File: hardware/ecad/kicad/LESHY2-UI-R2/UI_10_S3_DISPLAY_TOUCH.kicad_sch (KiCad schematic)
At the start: 35 parts, among them J1 Hirose FH34SRJ-50S-0.5SH(50), J2 Samtec FTSH-105-01-L-DV-K-P-TR, J3 GCT RFPC-SMA32-FN-175-A, J4 Hirose U.FL-R-SMT-1(80), SW1 Alps Alpine SKRTLAE010, SW2 Alps Alpine SKRTLAE010, U1 ESP32-S3-WROOM-1U-N16R8, U2 Texas Instruments TPD4E05U06D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, U3 KYOCERA AVX CP0603Q5425ENTR

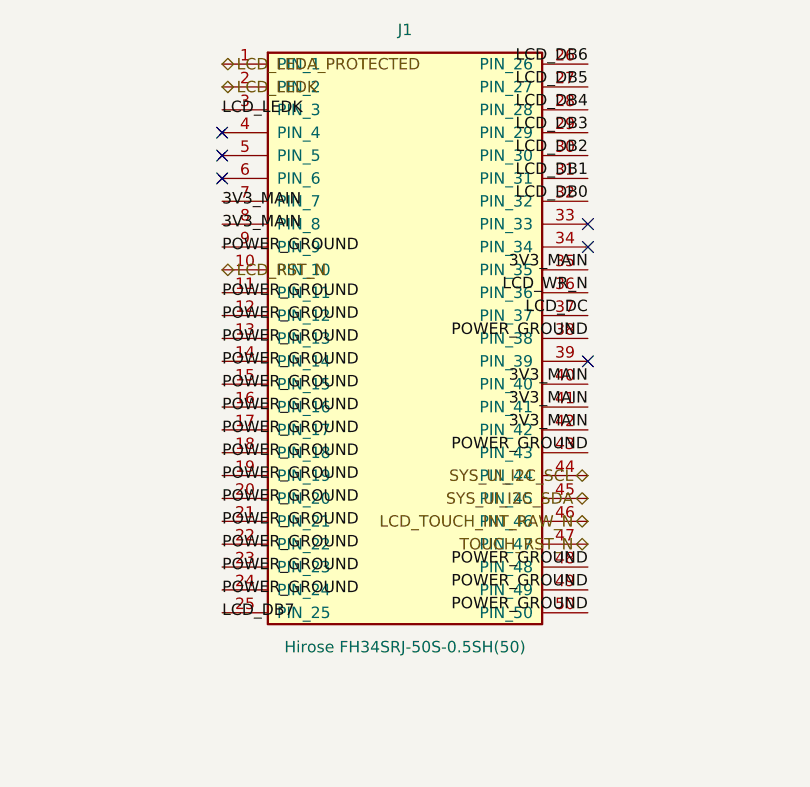
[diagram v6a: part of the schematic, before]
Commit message: Correct exact connector and protection geometry; expand electrical review
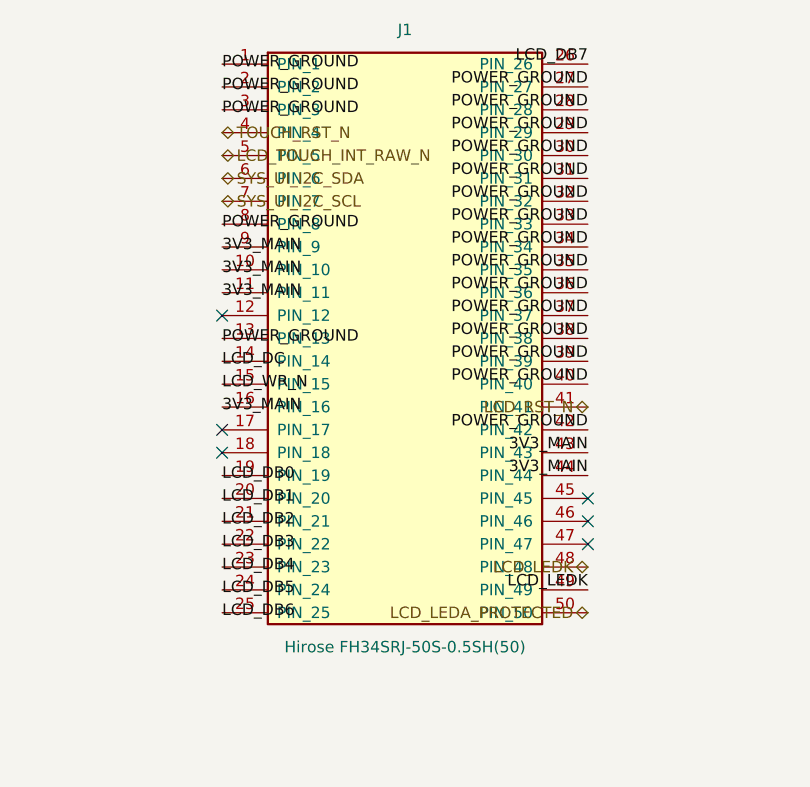
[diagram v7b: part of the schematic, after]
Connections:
- net 3V3_MAIN: now also J1.10 (PIN_10), J1.11 (PIN_11), J1.16 (PIN_16), J1.43 (PIN_43), J1.44 (PIN_44), J1.9 (PIN_9); no longer J1.35 (PIN_35), J1.40 (PIN_40), J1.41 (PIN_41), J1.42 (PIN_42), J1.7 (PIN_7), J1.8 (PIN_8)
- net LCD_DB0: now also J1.19 (PIN_19); no longer J1.32 (PIN_32)
- net LCD_DB1: now also J1.20 (PIN_20); no longer J1.31 (PIN_31)
- net LCD_DB2: now also J1.21 (PIN_21); no longer J1.30 (PIN_30)
- net LCD_DB3: now also J1.22 (PIN_22); no longer J1.29 (PIN_29)
- net LCD_DB4: now also J1.23 (PIN_23); no longer J1.28 (PIN_28)
- net LCD_DB5: now also J1.24 (PIN_24); no longer J1.27 (PIN_27)
- net LCD_DB6: now also J1.25 (PIN_25); no longer J1.26 (PIN_26)
- net LCD_DB7: now also J1.26 (PIN_26); no longer J1.25 (PIN_25)
- net LCD_DC: now also J1.14 (PIN_14); no longer J1.37 (PIN_37)
- net LCD_LEDA_PROTECTED: now also J1.50 (PIN_50); no longer J1.1 (PIN_1)
- net LCD_LEDK: now also J1.48 (PIN_48), J1.49 (PIN_49); no longer J1.2 (PIN_2), J1.3 (PIN_3)
- net LCD_RST_N: now also J1.41 (PIN_41); no longer J1.10 (PIN_10)
- net LCD_TOUCH_INT_RAW_N: now also J1.5 (PIN_5); no longer J1.46 (PIN_46)
- net LCD_WR_N: now also J1.15 (PIN_15); no longer J1.36 (PIN_36)
- net POWER_GROUND: now also J1.1 (PIN_1), J1.2 (PIN_2), J1.27 (PIN_27), J1.28 (PIN_28), J1.29 (PIN_29), J1.3 (PIN_3), J1.30 (PIN_30), J1.31 (PIN_31), J1.32 (PIN_32), J1.33 (PIN_33), J1.34 (PIN_34), J1.35 (PIN_35), J1.36 (PIN_36), J1.37 (PIN_37), J1.39 (PIN_39), J1.40 (PIN_40), J1.42 (PIN_42), J1.8 (PIN_8); no longer J1.11 (PIN_11), J1.12 (PIN_12), J1.14 (PIN_14), J1.15 (PIN_15), J1.16 (PIN_16), J1.17 (PIN_17), J1.18 (PIN_18), J1.19 (PIN_19), J1.20 (PIN_20), J1.21 (PIN_21), J1.22 (PIN_22), J1.23 (PIN_23), J1.24 (PIN_24), J1.43 (PIN_43), J1.48 (PIN_48), J1.49 (PIN_49), J1.50 (PIN_50), J1.9 (PIN_9)
- net SYS_UI_I2C_SCL: now also J1.7 (PIN_7); no longer J1.44 (PIN_44)
- net SYS_UI_I2C_SDA: now also J1.6 (PIN_6); no longer J1.45 (PIN_45)
- net TOUCH_RST_N: now also J1.4 (PIN_4); no longer J1.47 (PIN_47)
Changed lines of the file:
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@@
 		)
 	)
-	(hierarchical_label "LCD_LEDA_PROTECTED"
-		(shape bidirectional)
+	(label "POWER_GROUND"
 		(at 584.20 48.26 0)
 		(effects (font (size 1.27 1.27)))
 	)
-	(hierarchical_label "LCD_LEDK"
-		(shape bidirectional)
+	(label "POWER_GROUND"
 		(at 584.20 50.80 0)
 		(effects (font (size 1.27 1.27)))
 	)
-	(label "LCD_LEDK"
+	(label "POWER_GROUND"
 		(at 584.20 53.34 0)
 		(effects (font (size 1.27 1.27)))
 	)
-	(no_connect (at 584.20 55.88)
+	(hierarchical_label "TOUCH_RST_N"
+		(shape bidirectional)
+		(at 584.20 55.88 0)
+		(effects (font (size 1.27 1.27)))
 	)
-	(no_connect (at 584.20 58.42)
+	(hierarchical_label "LCD_TOUCH_INT_RAW_N"
+		(shape bidirectional)
+		(at 584.20 58.42 0)
+		(effects (font (size 1.27 1.27)))
 	)
-	(no_connect (at 584.20 60.96)
+	(hierarchical_label "SYS_UI_I2C_SDA"
+		(shape bidirectional)
+		(at 584.20 60.96 0)
+		(effects (font (size 1.27 1.27)))
 	)
-	(label "3V3_MAIN"
+	(hierarchical_label "SYS_UI_I2C_SCL"
+		(shape bidirectional)
 		(at 584.20 63.50 0)
 		(effects (font (size 1.27 1.27)))
 	)
-	(label "3V3_MAIN"
+	(label "POWER_GROUND"
 		(at 584.20 66.04 0)
 		(effects (font (size 1.27 1.27)))
 	)
-	(label "POWER_GROUND"
+	(label "3V3_MAIN"
 		(at 584.20 68.58 0)
 		(effects (font (size 1.27 1.27)))
 	)
-	(hierarchical_label "LCD_RST_N"
-		(shape bidirectional)
+	(label "3V3_MAIN"
 		(at 584.20 71.12 0)
 		(effects (font (size 1.27 1.27)))
 	)
-	(label "POWER_GROUND"
+	(label "3V3_MAIN"
 		(at 584.20 73.66 0)
 		(effects (font (size 1.27 1.27)))
 	)
-	(label "POWER_GROUND"
-		(at 584.20 76.20 0)
-		(effects (font (size 1.27 1.27)))
+	(no_connect (at 584.20 76.20)
 	)
 	(label "POWER_GROUND"
@@
 		(effects (font (size 1.27 1.27)))
 	)
-	(label "POWER_GROUND"
+	(label "LCD_DC"
 		(at 584.20 81.28 0)
 		(effects (font (size 1.27 1.27)))
 	)
-	(label "POWER_GROUND"
+	(label "LCD_WR_N"
 		(at 584.20 83.82 0)
 		(effects (font (size 1.27 1.27)))
 	)
-	(label "POWER_GROUND"
+	(label "3V3_MAIN"
 		(at 584.20 86.36 0)
 		(effects (font (size 1.27 1.27)))
 	)
-	(label "POWER_GROUND"
-		(at 584.20 88.90 0)
-		(effects (font (size 1.27 1.27)))
+	(no_connect (at 584.20 88.90)
 	)
-	(label "POWER_GROUND"
-		(at 584.20 91.44 0)
-		(effects (font (size 1.27 1.27)))
+	(no_connect (at 584.20 91.44)
 	)
-	(label "POWER_GROUND"
+	(label "LCD_DB0"
 		(at 584.20 93.98 0)
 		(effects (font (size 1.27 1.27)))
 	)
-	(label "POWER_GROUND"
+	(label "LCD_DB1"
 		(at 584.20 96.52 0)
 		(effects (font (size 1.27 1.27)))
 	)
-	(label "POWER_GROUND"
+	(label "LCD_DB2"
 		(at 584.20 99.06 0)
 		(effects (font (size 1.27 1.27)))
 	)
-	(label "POWER_GROUND"
+	(label "LCD_DB3"
 		(at 584.20 101.60 0)
 		(effects (font (size 1.27 1.27)))
 	)
-	(label "POWER_GROUND"
+	(label "LCD_DB4"
 		(at 584.20 104.14 0)
 		(effects (font (size 1.27 1.27)))
 	)
-	(label "POWER_GROUND"
+	(label "LCD_DB5"
 		(at 584.20 106.68 0)
 		(effects (font (size 1.27 1.27)))
 	)
-	(label "LCD_DB7"
+	(label "LCD_DB6"
 		(at 584.20 109.22 0)
 		(effects (font (size 1.27 1.27)))
 	)
-	(label "LCD_DB6"
+	(label "LCD_DB7"
 		(at 624.84 48.26 180)
 		(effects (font (size 1.27 1.27)) (justify right bottom))
 	)
-	(label "LCD_DB5"
+	(label "POWER_GROUND"
 		(at 624.84 50.80 180)
 		(effects (font (size 1.27 1.27)) (justify right bottom))
 	)
-	(label "LCD_DB4"
+	(label "POWER_GROUND"
 		(at 624.84 53.34 180)
 		(effects (font (size 1.27 1.27)) (justify right bottom))
 	)
-	(label "LCD_DB3"
+	(label "POWER_GROUND"
 		(at 624.84 55.88 180)
 		(effects (font (size 1.27 1.27)) (justify right bottom))
 	)
-	(label "LCD_DB2"
+	(label "POWER_GROUND"
 		(at 624.84 58.42 180)
 		(effects (font (size 1.27 1.27)) (justify right bottom))
 	)
-	(label "LCD_DB1"
+	(label "POWER_GROUND"
 		(at 624.84 60.96 180)
 		(effects (font (size 1.27 1.27)) (justify right bottom))
 	)
-	(label "LCD_DB0"
+	(label "POWER_GROUND"
 		(at 624.84 63.50 180)
 		(effects (font (size 1.27 1.27)) (justify right bottom))
 	)
-	(no_connect (at 624.84 66.04)
+	(label "POWER_GROUND"
+		(at 624.84 66.04 180)
+		(effects (font (size 1.27 1.27)) (justify right bottom))
 	)
-	(no_connect (at 624.84 68.58)
+	(label "POWER_GROUND"
+		(at 624.84 68.58 180)
+		(effects (font (size 1.27 1.27)) (justify right bottom))
 	)
-	(label "3V3_MAIN"
+	(label "POWER_GROUND"
 		(at 624.84 71.12 180)
 		(effects (font (size 1.27 1.27)) (justify right bottom))
 	)
-	(label "LCD_WR_N"
+	(label "POWER_GROUND"
 		(at 624.84 73.66 180)
 		(effects (font (size 1.27 1.27)) (justify right bottom))
 	)
-	(label "LCD_DC"
+	(label "POWER_GROUND"
 		(at 624.84 76.20 180)
 		(effects (font (size 1.27 1.27)) (justify right bottom))
@@
 		(effects (font (size 1.27 1.27)) (justify right bottom))
 	)
-	(no_connect (at 624.84 81.28)
+	(label "POWER_GROUND"
+		(at 624.84 81.28 180)
+		(effects (font (size 1.27 1.27)) (justify right bottom))
 	)
-	(label "3V3_MAIN"
+	(label "POWER_GROUND"
 		(at 624.84 83.82 180)
 		(effects (font (size 1.27 1.27)) (justify right bottom))
 	)
-	(label "3V3_MAIN"
+	(hierarchical_label "LCD_RST_N"
+		(shape bidirectional)
 		(at 624.84 86.36 180)
 		(effects (font (size 1.27 1.27)) (justify right bottom))
 	)
-	(label "3V3_MAIN"
+	(label "POWER_GROUND"
 		(at 624.84 88.90 180)
 		(effects (font (size 1.27 1.27)) (justify right bottom))
 	)
-	(label "POWER_GROUND"
+	(label "3V3_MAIN"
 		(at 624.84 91.44 180)
 		(effects (font (size 1.27 1.27)) (justify right bottom))
 	)
-	(hierarchical_label "SYS_UI_I2C_SCL"
-		(shape bidirectional)
+	(label "3V3_MAIN"
 		(at 624.84 93.98 180)
 		(effects (font (size 1.27 1.27)) (justify right bottom))
 	)
-	(hierarchical_label "SYS_UI_I2C_SDA"
+	(no_connect (at 624.84 96.52)
+	)
+	(no_connect (at 624.84 99.06)
+	)
+	(no_connect (at 624.84 101.60)
+	)
+	(hierarchical_label "LCD_LEDK"
 		(shape bidirectional)
-		(at 624.84 96.52 180)
-		(effects (font (size 1.27 1.27)) (justify right bottom))
-	)
-	(hierarchical_label "LCD_TOUCH_INT_RAW_N"
-		(shape bidirectional)
-		(at 624.84 99.06 180)
-		(effects (font (size 1.27 1.27)) (justify right bottom))
-	)
-	(hierarchical_label "TOUCH_RST_N"
-		(shape bidirectional)
-		(at 624.84 101.60 180)
-		(effects (font (size 1.27 1.27)) (justify right bottom))
-	)
-	(label "POWER_GROUND"
 		(at 624.84 104.14 180)
 		(effects (font (size 1.27 1.27)) (justify right bottom))
 	)
-	(label "POWER_GROUND"
+	(label "LCD_LEDK"
 		(at 624.84 106.68 180)
 		(effects (font (size 1.27 1.27)) (justify right bottom))
 	)
-	(label "POWER_GROUND"
+	(hierarchical_label "LCD_LEDA_PROTECTED"
+		(shape bidirectional)
 		(at 624.84 109.22 180)
 		(effects (font (size 1.27 1.27)) (justify right bottom))

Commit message: Correct exact RF lands and reopen native power prerequisites
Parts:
- U3: footprint Leshy2:CP0603Q5425ENTR -> Leshy2_R2:CP0603Q5425ENTR
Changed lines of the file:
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@@
 			(effects (font (size 1.27 1.27)))
 		)
-		(property "Footprint" "Leshy2:CP0603Q5425ENTR"
+		(property "Footprint" "Leshy2_R2:CP0603Q5425ENTR"
 			(at 604.52 140.97 0)
 			(show_name no)
